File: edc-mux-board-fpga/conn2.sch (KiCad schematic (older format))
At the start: 24 parts, among them U10 MAX4910, U11 TLV320AIC3206, U12 P82B96

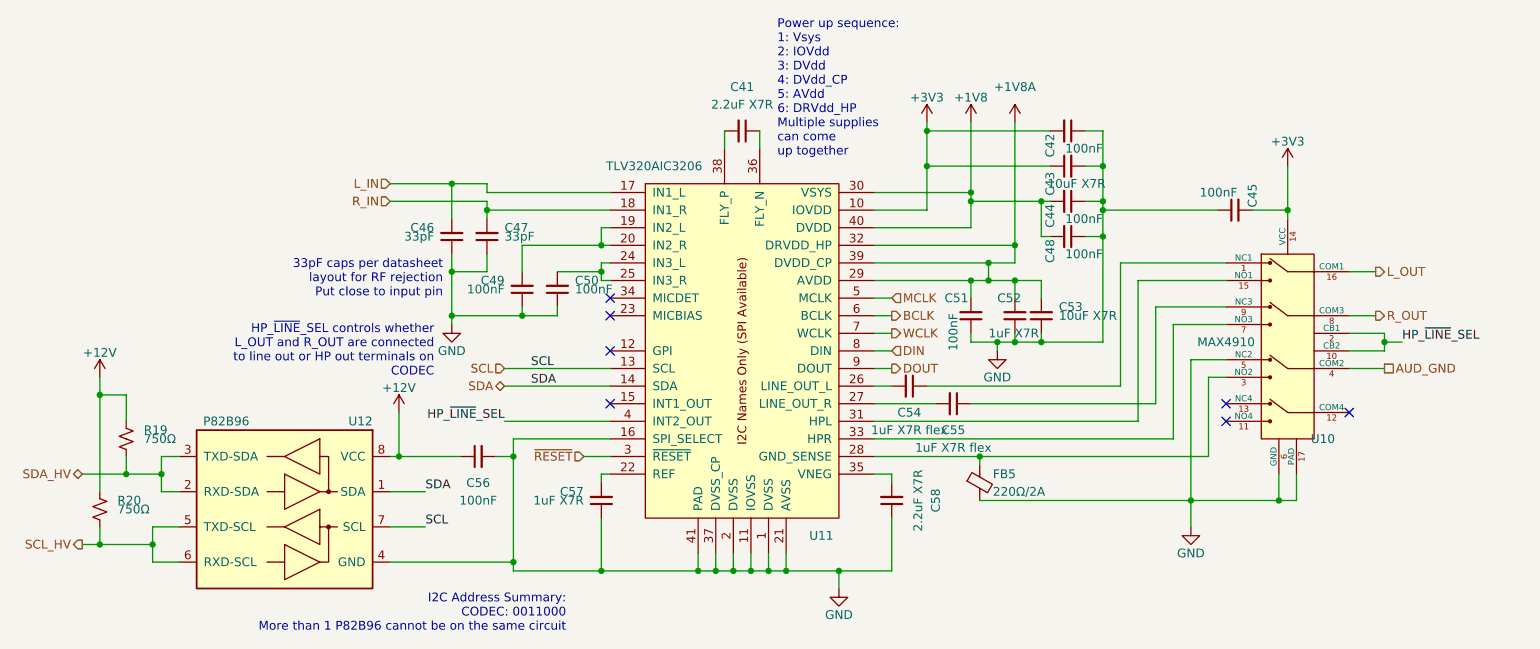
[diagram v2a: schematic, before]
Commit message: re-annotating after adding power ICs and decoupling capacitors.
Also verified most footprints, and updated schematic field data.
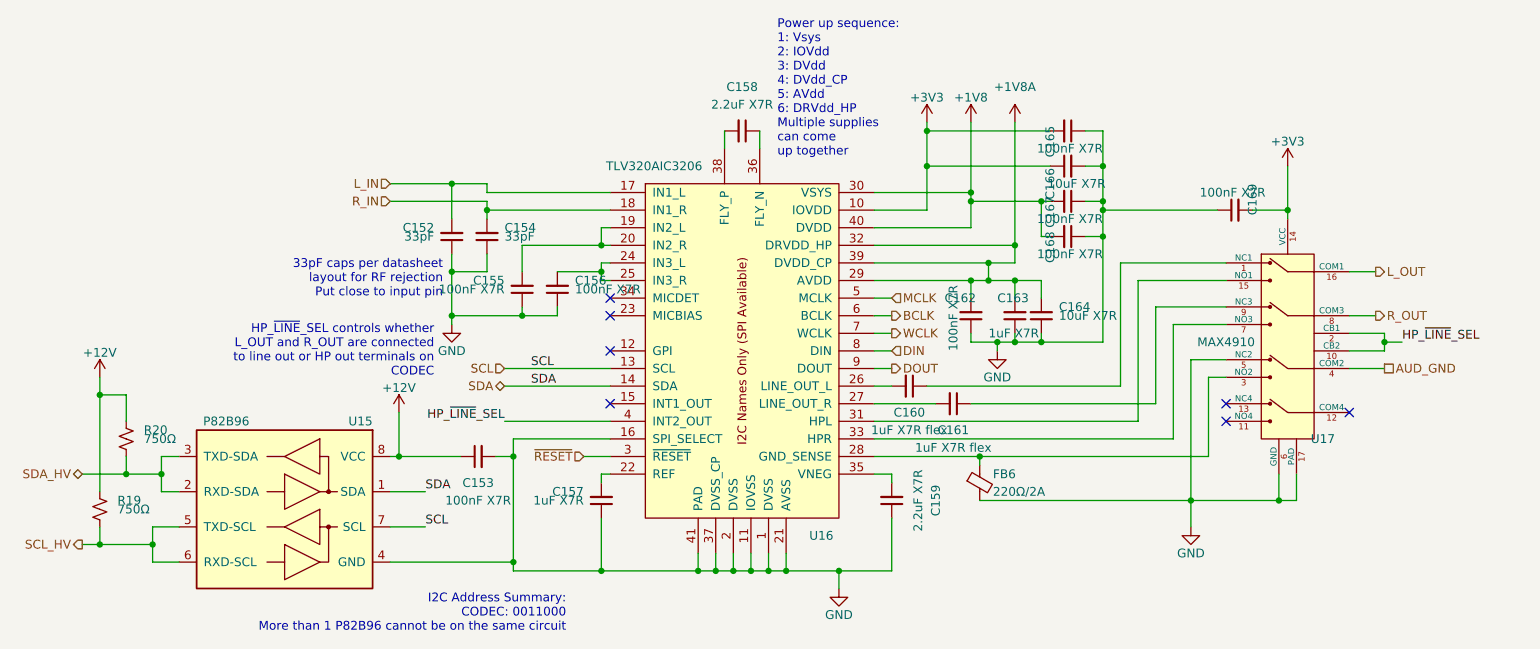
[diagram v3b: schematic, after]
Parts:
- C153: renamed from C56; value 100nF -> 100nF X7R
- C155: renamed from C49; value 100nF -> 100nF X7R
- C156: renamed from C50; value 100nF -> 100nF X7R
- C162: renamed from C51; value 100nF -> 100nF X7R
- C165: renamed from C42; value 100nF -> 100nF X7R
- C167: renamed from C44; value 100nF -> 100nF X7R
- C168: renamed from C48; value 100nF -> 100nF X7R
- C169: renamed from C45; value 100nF -> 100nF X7R
- R19: renamed from R20; Package ID (none) -> 0402in/1005mm
- R20: renamed from R19; Package ID (none) -> 0402in/1005mm
- renumbered C46 to C152, C47 to C154, C57 to C157, C41 to C158, C58 to C159, C54 to C160, C55 to C161, C52 to C163, C53 to C164, C43 to C166, FB5 to FB6, U12 to U15, U11 to U16, U10 to U17

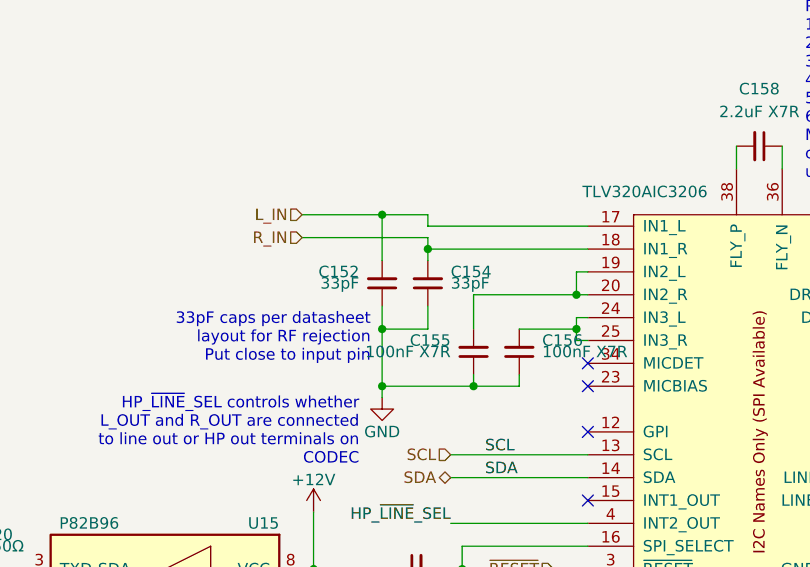
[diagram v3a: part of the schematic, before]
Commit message: Reannotating and adding more fields to components
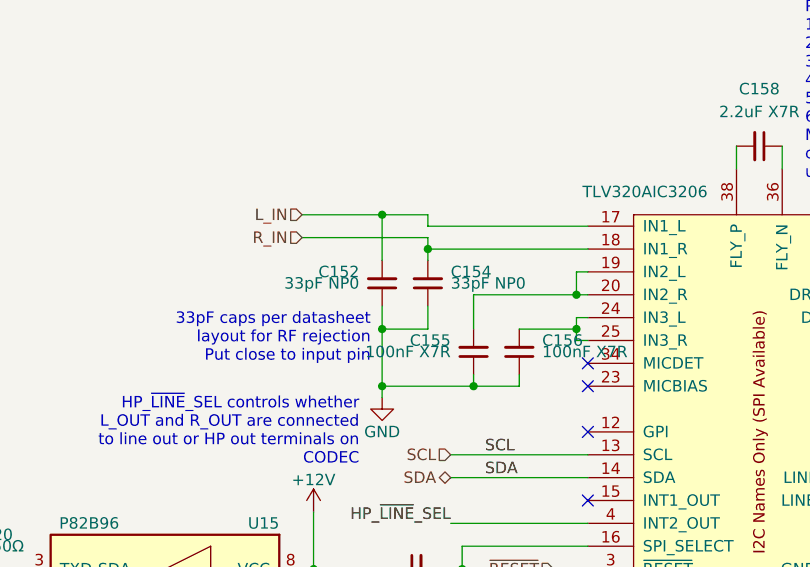
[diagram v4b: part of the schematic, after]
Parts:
- C152, C154: value 33pF -> 33pF NP0; footprint Capacitor_SMD:C_0603_1608Metric -> Capacitor_SMD:C_0402_1005Metric; Characteristics (none) -> CAP CER 33PF 25V NP0 0402; Description (none) -> MLCC Capacitor; Manufacturer (none) -> AVX; Manufacturers Part Number (none) -> 04023A330FAT2A; Package ID 0603in/1608mm -> 0402in/1005mm
- C153, C155, C156, C162, C165, C167, C168, C169: Characteristics (none) -> CAP CER 0.1UF 25V X7R 0603; Description (none) -> MLCC Capacitor; Manufacturer (none) -> Kemet; Manufacturers Part Number (none) -> C0603C104J3RACAUTO
- C157, C163: Characteristics (none) -> CAP CER 1UF 25V X7R 0603; Description (none) -> MLCC Capacitor
- C158, C159: footprint Capacitor_SMD:C_0603_1608Metric -> Capacitor_SMD:C_0805_2012Metric; Characteristics (none) -> CAP CER 2.2UF 25V X7R 0805; Description (none) -> MLCC Capacitor; Manufacturer (none) -> TDK; Manufacturers Part Number (none) -> CGA4J3X7R1E225K125AB; Package ID 0603in/1608mm -> 0805in/2012mm
- C160, C161: Characteristics (none) -> CAP CER 0805 1UF 25V X7R 5%; Description (none) -> MLCC Capacitor; Manufacturers Part Number C0805X105J3RACAUTO -> C0805X105J3RECAUTO
- C164, C166: Characteristics (none) -> CAP CER 10UF 25V X7R 1206; Description (none) -> MLCC Capacitor
- FB6: footprint Resistor_SMD:R_0603_1608Metric -> Inductor_SMD:L_0603_1608Metric; Description (none) -> Ferrite Bead
- R19, R20: Description (none) -> Resistor
- U15: Description (none) -> I2C Buffer / Voltage Translator; Manufacturer (none) -> Texas Instruments; Manufacturers Part Number (none) -> P82B96; Package ID (none) -> TSSOP8
- U16: Description (none) -> I2S Audio Codec; Manufacturer (none) -> Texas Instruments; Package ID (none) -> UQFN40
- U17: Description (none) -> Clickless Audio Switch; Manufacturer (none) -> Maxim Integrated; Package ID (none) -> TQFN16

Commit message: Fixed resistor footprint
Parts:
- R19, R20: footprint Resistor_SMD:R_0603_1608Metric -> Resistor_SMD:R_0402_1005Metric
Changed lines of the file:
@@
 F 0 "R20" H 1800 3950 50  0000 L CNN
 F 1 "750Ω" H 1800 3900 50  0000 L CNN
-F 2 "Resistor_SMD:R_0603_1608Metric" H 1700 3900 50  0001 C CNN
+F 2 "Resistor_SMD:R_0402_1005Metric" H 1700 3900 50  0001 C CNN
 F 3 "~" H 1700 3900 50  0001 C CNN
 F 4 "0402in/1005mm" H 0   0   50  0001 C CNN "Package ID"
@@
 F 0 "R19" H 1650 4350 50  0000 L CNN
 F 1 "750Ω" H 1650 4300 50  0000 L CNN
-F 2 "Resistor_SMD:R_0603_1608Metric" H 1550 4300 50  0001 C CNN
+F 2 "Resistor_SMD:R_0402_1005Metric" H 1550 4300 50  0001 C CNN
 F 3 "~" H 1550 4300 50  0001 C CNN
 F 4 "0402in/1005mm" H 0   0   50  0001 C CNN "Package ID"
